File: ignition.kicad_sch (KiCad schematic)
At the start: 14 parts, among them J2 Centroid, Q1 PMOS-GSD, Q2 Q_NMOS_GSD, U4 CPC1135N

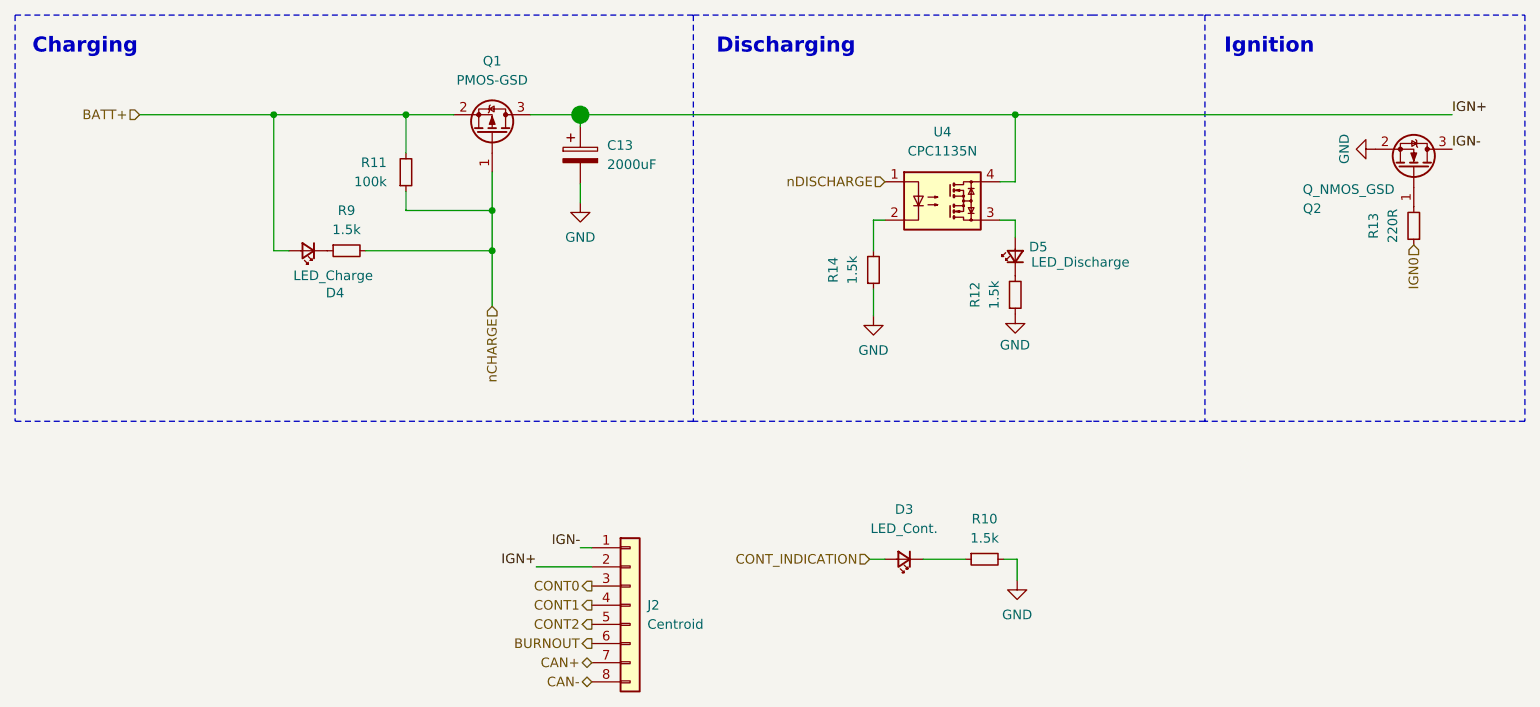
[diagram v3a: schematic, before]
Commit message: #1 New pyro channel introduced in schematic
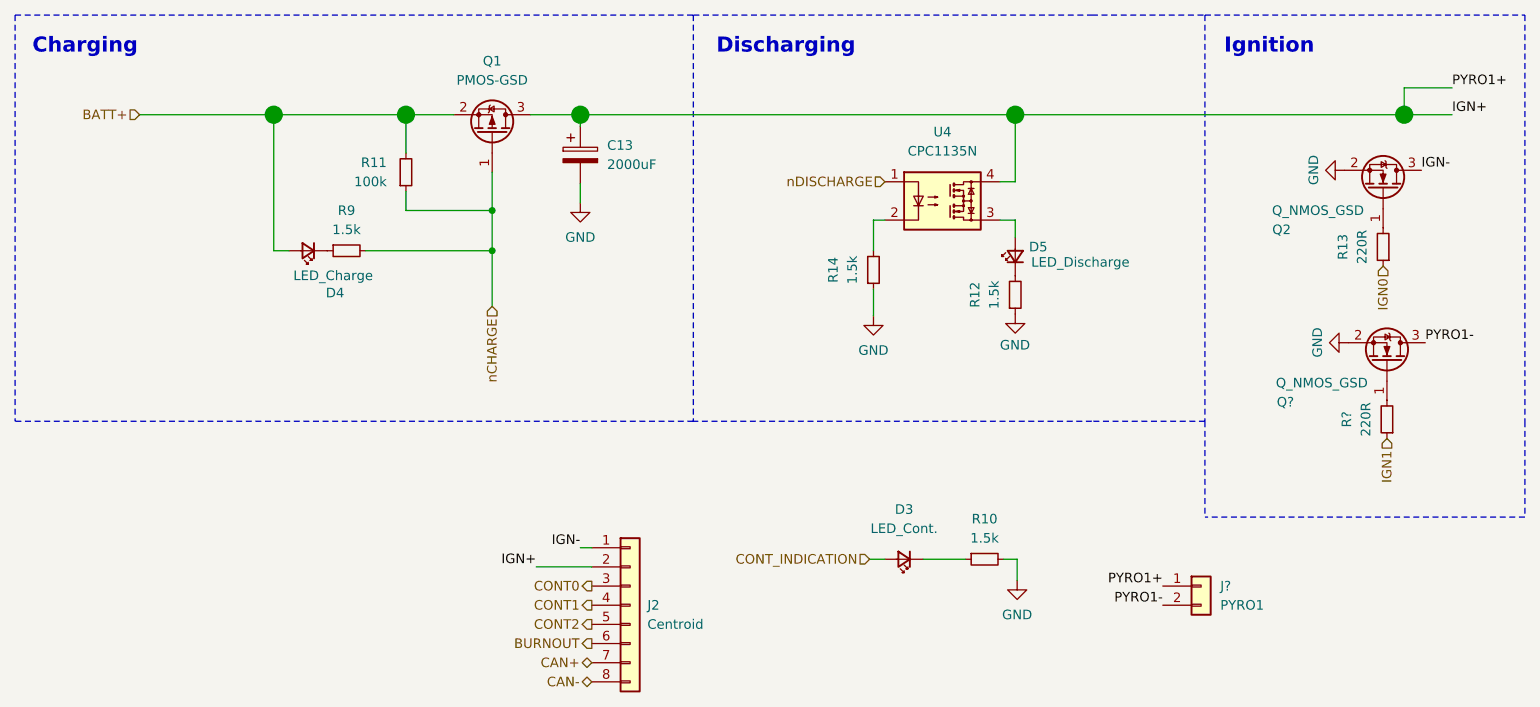
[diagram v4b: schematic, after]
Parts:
- added J?: PYRO1, symbol Connector_Generic:Conn_01x02
- added Q?: Q_NMOS_GSD, Package_TO_SOT_SMD:SOT-23, symbol Device:Q_NMOS_GSD
- added R?: 220R, Resistor_SMD:R_0402_1005Metric, symbol Device:R_Small
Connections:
- net GND: now also Q?.2 (S)
- net IGN+: now also J?.1 (Pin_1)
- new net: Q?.1 (G), R?.2
- new net IGN1: R?.1
- new net PYRO1-: J?.2 (Pin_2), Q?.3 (D)
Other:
- moved on the sheet: Q2, R13
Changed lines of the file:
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@@
 (kicad_sch (version 20210621) (generator eeschema)
   (paper "A4")
-  (junction (at 81.534 52.832) (diameter 0.9144) (color 0 0 0 0))
-  (junction (at 99.06 52.832) (diameter 0.9144) (color 0 0 0 0))
+  (junction (at 81.534 52.832) (diameter 2.4136) (color 0 0 0 0))
+  (junction (at 99.06 52.832) (diameter 2.4136) (color 0 0 0 0))
   (junction (at 110.49 65.532) (diameter 0.9144) (color 0 0 0 0))
   (junction (at 110.49 70.866) (diameter 0.9144) (color 0 0 0 0))
   (junction (at 122.174 52.832) (diameter 2.4136) (color 0 0 0 0))
-  (junction (at 179.832 52.832) (diameter 0.9144) (color 0 0 0 0))
+  (junction (at 179.832 52.832) (diameter 2.4136) (color 0 0 0 0))
+  (junction (at 231.394 52.832) (diameter 2.4136) (color 0 0 0 0))
   (wire (pts (xy 63.754 52.832) (xy 81.534 52.832))
     (stroke (width 0) (type solid) (color 0 0 0 0))
@@
     (stroke (width 0) (type solid) (color 0 0 0 0))
   )
-  (wire (pts (xy 179.832 52.832) (xy 237.744 52.832))
+  (wire (pts (xy 179.832 52.832) (xy 231.394 52.832))
     (stroke (width 0) (type solid) (color 0 0 0 0))
   )
@@
     (stroke (width 0) (type solid) (color 0 0 0 0))
   )
+  (wire (pts (xy 231.394 49.276) (xy 231.394 52.832))
+    (stroke (width 0) (type solid) (color 0 0 0 0))
+  )
+  (wire (pts (xy 231.394 52.832) (xy 237.744 52.832))
+    (stroke (width 0) (type solid) (color 0 0 0 0))
+  )
+  (wire (pts (xy 237.744 49.276) (xy 231.394 49.276))
+    (stroke (width 0) (type solid) (color 0 0 0 0))
+  )
   (polyline (pts (xy 47.244 39.624) (xy 47.244 93.472))
     (stroke (width 0) (type dash) (color 0 0 0 0))
@@
     (stroke (width 0) (type dash) (color 0 0 0 0))
   )
+  (polyline (pts (xy 204.978 93.472) (xy 204.978 106.172))
+    (stroke (width 0) (type dash) (color 0 0 0 0))
+  )
   (polyline (pts (xy 247.396 39.624) (xy 247.396 93.472))
     (stroke (width 0) (type dash) (color 0 0 0 0))
   )
-  (polyline (pts (xy 247.396 93.472) (xy 204.978 93.472))
+  (polyline (pts (xy 247.396 93.472) (xy 247.396 106.172))
+    (stroke (width 0) (type dash) (color 0 0 0 0))
+  )
+  (polyline (pts (xy 247.396 106.172) (xy 204.978 106.172))
     (stroke (width 0) (type dash) (color 0 0 0 0))
   )
@@
     (effects (font (size 1.27 1.27)) (justify right bottom))
   )
+  (label "PYRO1+" (at 199.39 115.316 180)
+    (effects (font (size 1.27 1.27)) (justify right bottom))
+  )
+  (label "PYRO1-" (at 199.39 117.856 180)
+    (effects (font (size 1.27 1.27)) (justify right bottom))
+  )
+  (label "IGN-" (at 233.68 60.198 0)
+    (effects (font (size 1.27 1.27)) (justify left bottom))
+  )
+  (label "PYRO1-" (at 234.188 83.058 0)
+    (effects (font (size 1.27 1.27)) (justify left bottom))
+  )
+  (label "PYRO1+" (at 237.744 49.276 0)
+    (effects (font (size 1.27 1.27)) (justify left bottom))
+  )
   (label "IGN+" (at 237.744 52.832 0)
     (effects (font (size 1.27 1.27)) (justify left bottom))
   )
-  (label "IGN-" (at 237.744 57.404 0)
-    (effects (font (size 1.27 1.27)) (justify left bottom))
-  )
   (hierarchical_label "BATT+" (shape input) (at 63.754 52.832 180)
     (effects (font (size 1.27 1.27)) (justify right))
@@
     (effects (font (size 1.27 1.27)) (justify right))
   )
-  (hierarchical_label "IGN0" (shape input) (at 232.664 70.104 270)
+  (hierarchical_label "IGN0" (shape input) (at 228.6 72.898 270)
+    (effects (font (size 1.27 1.27)) (justify right))
+  )
+  (hierarchical_label "IGN1" (shape input) (at 229.108 95.758 270)
     (effects (font (size 1.27 1.27)) (justify right))
   )
@@
     (pin "1")
   )
-  (symbol (lib_id "power:GND") (at 227.584 57.404 270) (unit 1)
-    (in_bom yes) (on_board yes)
-    (property "Reference" "#PWR019" (id 0) (at 221.234 57.404 0)
-      (effects (font (size 1.27 1.27)) hide)
-    )
-    (property "Value" "GND" (id 1) (at 223.4566 55.372 0)
-      (effects (font (size 1.27 1.27)) (justify left))
-    )
-    (property "Footprint" "" (id 2) (at 227.584 57.404 0)
-      (effects (font (size 1.27 1.27)) hide)
-    )
-    (property "Datasheet" "" (id 3) (at 227.584 57.404 0)
+  (symbol (lib_id "power:GND") (at 223.52 60.198 270) (unit 1)
+    (in_bom yes) (on_board yes)
+    (property "Reference" "#PWR019" (id 0) (at 217.17 60.198 0)
+      (effects (font (size 1.27 1.27)) hide)
+    )
+    (property "Value" "GND" (id 1) (at 219.3926 58.166 0)
+      (effects (font (size 1.27 1.27)) (justify left))
+    )
+    (property "Footprint" "" (id 2) (at 223.52 60.198 0)
+      (effects (font (size 1.27 1.27)) hide)
+    )
+    (property "Datasheet" "" (id 3) (at 223.52 60.198 0)
+      (effects (font (size 1.27 1.27)) hide)
+    )
+    (pin "1")
+  )
+  (symbol (lib_id "power:GND") (at 224.028 83.058 270) (unit 1)
+    (in_bom yes) (on_board yes)
+    (property "Reference" "#PWR?" (id 0) (at 217.678 83.058 0)
+      (effects (font (size 1.27 1.27)) hide)
+    )
+    (property "Value" "GND" (id 1) (at 219.9006 81.026 0)
+      (effects (font (size 1.27 1.27)) (justify left))
+    )
+    (property "Footprint" "" (id 2) (at 224.028 83.058 0)
+      (effects (font (size 1.27 1.27)) hide)
+    )
+    (property "Datasheet" "" (id 3) (at 224.028 83.058 0)
       (effects (font (size 1.27 1.27)) hide)
     )
@@
     (pin "2")
   )
-  (symbol (lib_id "Device:R_Small") (at 232.664 67.564 180) (unit 1)
-    (in_bom yes) (on_board yes) (fields_autoplaced)
-    (property "Reference" "R13" (id 0) (at 227.33 67.564 90))
-    (property "Value" "220R" (id 1) (at 229.87 67.564 90))
-    (property "Footprint" "Resistor_SMD:R_0402_1005Metric" (id 2) (at 232.664 67.564 0)
-      (effects (font (size 1.27 1.27)) hide)
-    )
-    (property "Datasheet" "~" (id 3) (at 232.664 67.564 0)
+  (symbol (lib_id "Device:R_Small") (at 228.6 70.358 180) (unit 1)
+    (in_bom yes) (on_board yes) (fields_autoplaced)
+    (property "Reference" "R13" (id 0) (at 223.266 70.358 90))
+    (property "Value" "220R" (id 1) (at 225.806 70.358 90))
+    (property "Footprint" "Resistor_SMD:R_0402_1005Metric" (id 2) (at 228.6 70.358 0)
+      (effects (font (size 1.27 1.27)) hide)
+    )
+    (property "Datasheet" "~" (id 3) (at 228.6 70.358 0)
+      (effects (font (size 1.27 1.27)) hide)
+    )
+    (pin "1")
+    (pin "2")
+  )
+  (symbol (lib_id "Device:R_Small") (at 229.108 93.218 180) (unit 1)
+    (in_bom yes) (on_board yes) (fields_autoplaced)
+    (property "Reference" "R?" (id 0) (at 223.774 93.218 90))
+    (property "Value" "220R" (id 1) (at 226.314 93.218 90))
+    (property "Footprint" "Resistor_SMD:R_0402_1005Metric" (id 2) (at 229.108 93.218 0)
+      (effects (font (size 1.27 1.27)) hide)
+    )
+    (property "Datasheet" "~" (id 3) (at 229.108 93.218 0)
       (effects (font (size 1.27 1.27)) hide)
     )
@@
     (pin "2")
   )
+  (symbol (lib_id "Connector_Generic:Conn_01x02") (at 204.47 115.316 0) (unit 1)
+    (in_bom yes) (on_board yes) (fields_autoplaced)
+    (property "Reference" "J?" (id 0) (at 207.01 115.3159 0)
+      (effects (font (size 1.27 1.27)) (justify left))
+    )
+    (property "Value" "PYRO1" (id 1) (at 207.01 117.8559 0)
+      (effects (font (size 1.27 1.27)) (justify left))
+    )
+    (property "Footprint" "" (id 2) (at 204.47 115.316 0)
+      (effects (font (size 1.27 1.27)) hide)
+    )
+    (property "Datasheet" "~" (id 3) (at 204.47 115.316 0)
+      (effects (font (size 1.27 1.27)) hide)
+    )
+    (pin "1")
+    (pin "2")
+  )
   (symbol (lib_id "Device:C_Polarized") (at 122.174 58.166 0) (unit 1)
     (in_bom yes) (on_board yes) (fields_autoplaced)
@@
     (pin "3")
   )
-  (symbol (lib_id "Device:Q_NMOS_GSD") (at 232.664 59.944 270) (mirror x) (unit 1)
-    (in_bom yes) (on_board yes)
-    (property "Reference" "Q2" (id 0) (at 219.202 65.278 90))
-    (property "Value" "Q_NMOS_GSD" (id 1) (at 224.028 62.738 90))
-    (property "Footprint" "Package_TO_SOT_SMD:SOT-23" (id 2) (at 235.204 54.864 0)
-      (effects (font (size 1.27 1.27)) hide)
-    )
-    (property "Datasheet" "~" (id 3) (at 232.664 59.944 0)
-      (effects (font (size 1.27 1.27)) hide)
-    )
+  (symbol (lib_id "Device:Q_NMOS_GSD") (at 228.6 62.738 270) (mirror x) (unit 1)
+    (in_bom yes) (on_board yes)
+    (property "Reference" "Q2" (id 0) (at 215.138 68.072 90))
+    (property "Value" "Q_NMOS_GSD" (id 1) (at 219.964 65.532 90))
+    (property "Footprint" "Package_TO_SOT_SMD:SOT-23" (id 2) (at 231.14 57.658 0)
+      (effects (font (size 1.27 1.27)) hide)
+    )
+    (property "Datasheet" "~" (id 3) (at 228.6 62.738 0)
+      (effects (font (size 1.27 1.27)) hide)
+    )
+    (pin "1")
+    (pin "2")
+    (pin "3")
+  )
+  (symbol (lib_id "Device:Q_NMOS_GSD") (at 229.108 85.598 270) (mirror x) (unit 1)
+    (in_bom yes) (on_board yes)
+    (property "Reference" "Q?" (id 0) (at 215.646 90.932 90))
+    (property "Value" "Q_NMOS_GSD" (id 1) (at 220.472 88.392 90))
+    (property "Footprint" "Package_TO_SOT_SMD:SOT-23" (id 2) (at 231.648 80.518 0)
+      (effects (font (size 1.27 1.27)) hide)
+    )
+    (property "Datasheet" "~" (id 3) (at 229.108 85.598 0)
+      (effects (font (size 1.27 1.27)) hide)
+    )

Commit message: Apply schematic updates to PCB
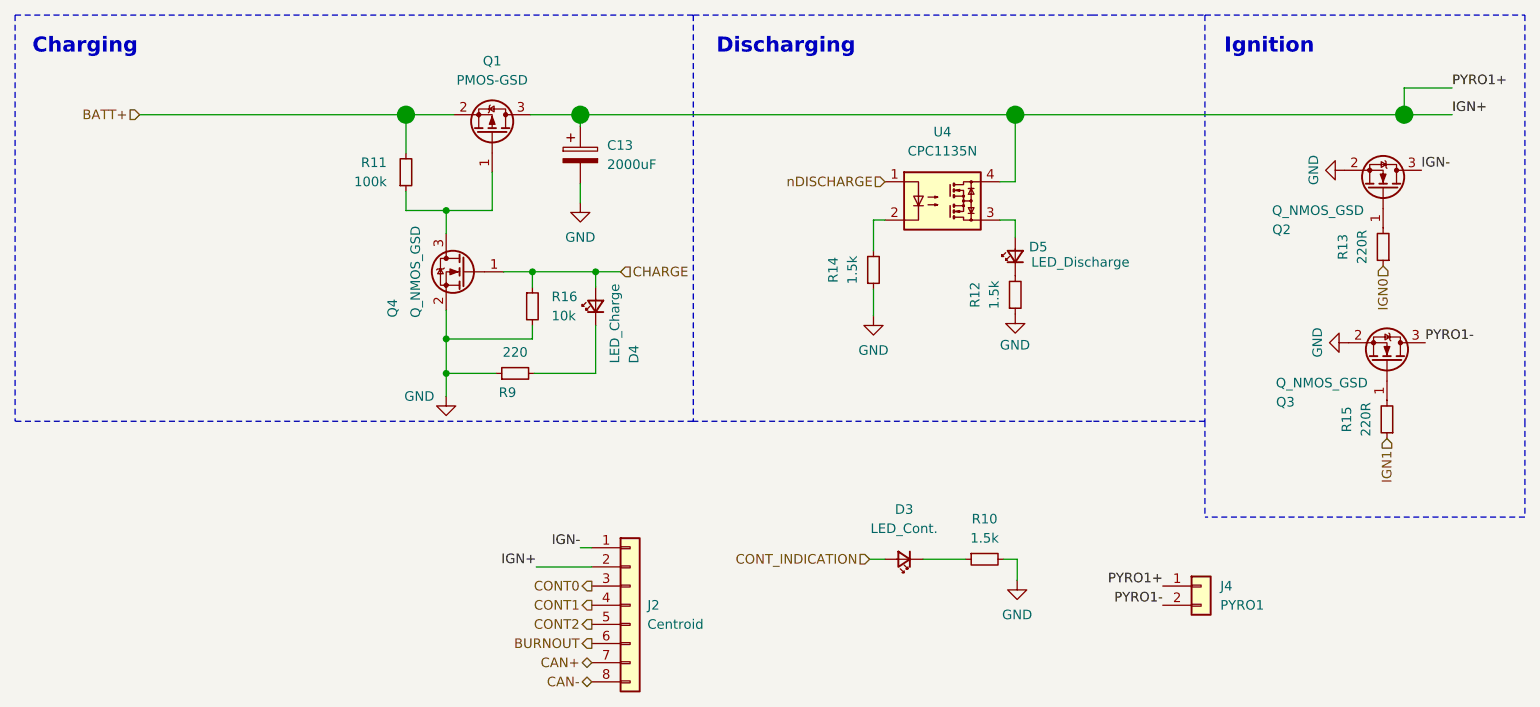
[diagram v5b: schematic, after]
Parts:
- added Q4: Q_NMOS_GSD, Package_TO_SOT_SMD:SOT-23, symbol Device:Q_NMOS_GSD
- added R16: 10k, Resistor_SMD:R_0402_1005Metric, symbol Device:R_Small
- J4: renamed from J?; footprint (none) -> Connector_PinHeader_2.54mm:PinHeader_1x02_P2.54mm_Vertical_SMD_Pin1Left
- R11: footprint (none) -> Resistor_SMD:R_0402_1005Metric
- R9: value 1.5k -> 220
- gave numbers to parts that had none: 2
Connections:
- net BATT+: no longer D4.2 (A)
- net GND: now also R9.1, Q4.2 (S), R16.2
- net at D4.1 (K): now also R9.2; no longer R9.1
- net nCHARGE: no longer names the net of Q1.1 (G), R11.1
- net nCHARGE: now also Q4.3 (D); no longer R9.2
- new net CHARGE: D4.2 (A), Q4.1 (G), R16.1
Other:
- moved on the sheet: D4

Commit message: Bump to Rev.3
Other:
- company: (none) -> Badger
- title: (none) -> Badger-Pike: Engine Control Module
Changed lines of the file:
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@@
 (kicad_sch (version 20210621) (generator eeschema)
   (paper "A4")
-  (junction (at 99.06 52.832) (diameter 2.4136) (color 0 0 0 0))
+  (title_block
+    (title "Badger-Pike: Engine Control Module")
+    (date "2021-09-01")
+    (rev "Rev. 3")
+    (company "Badger")
+  )
+  (junction (at 99.06 52.832) (diameter 0.9144) (color 0 0 0 0))
   (junction (at 104.394 65.532) (diameter 0.9144) (color 0 0 0 0))
   (junction (at 104.394 82.55) (diameter 0.9144) (color 0 0 0 0))
@@
   (junction (at 122.174 52.832) (diameter 2.4136) (color 0 0 0 0))
   (junction (at 124.206 73.66) (diameter 0.9144) (color 0 0 0 0))
-  (junction (at 179.832 52.832) (diameter 2.4136) (color 0 0 0 0))
-  (junction (at 231.394 52.832) (diameter 2.4136) (color 0 0 0 0))
+  (junction (at 179.832 52.832) (diameter 0.9144) (color 0 0 0 0))
+  (junction (at 231.394 52.832) (diameter 0.9144) (color 0 0 0 0))
   (wire (pts (xy 63.754 52.832) (xy 99.06 52.832))
     (stroke (width 0) (type solid) (color 0 0 0 0))
